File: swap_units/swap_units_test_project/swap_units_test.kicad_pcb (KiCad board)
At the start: 2 copper layers, 12 parts, among them U1 LM324, U2 PIC18F452-IP, U3 LM324

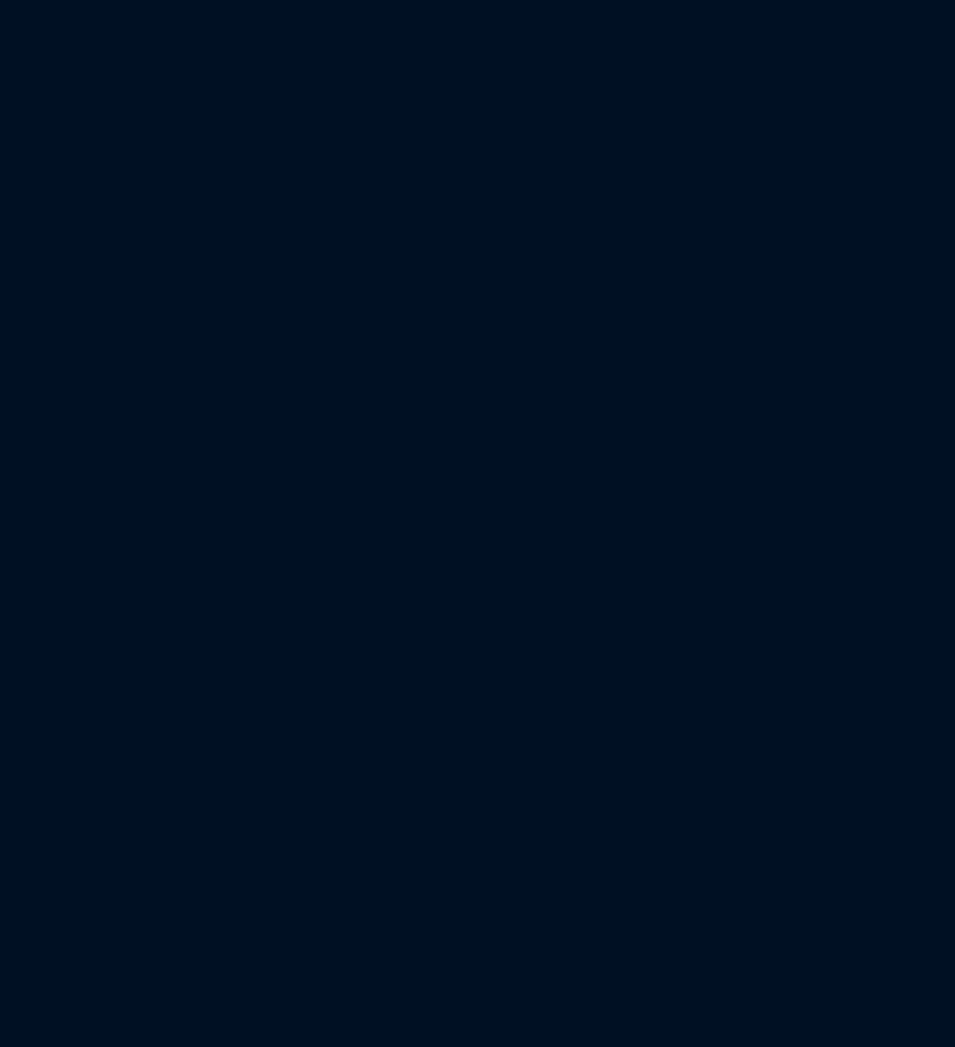
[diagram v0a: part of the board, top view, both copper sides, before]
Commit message: Moved and modified test project
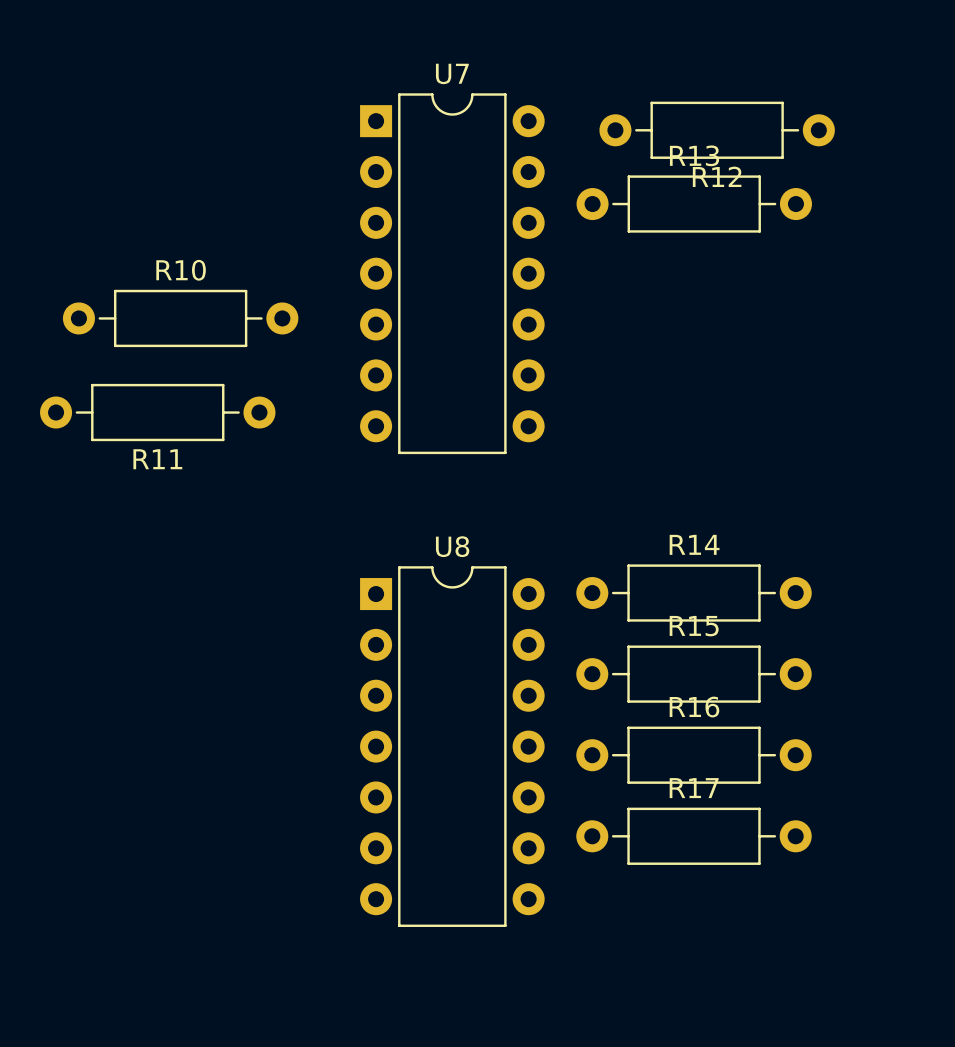
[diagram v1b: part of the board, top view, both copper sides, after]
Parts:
- added R10: R, Resistor_THT:R_Axial_DIN0207_L6.3mm_D2.5mm_P10.16mm_Horizontal, F.Cu at (21.1, 62.4)
- added R11: R, Resistor_THT:R_Axial_DIN0207_L6.3mm_D2.5mm_P10.16mm_Horizontal, F.Cu at (30.1, 67.1)
- added R12: R, Resistor_THT:R_Axial_DIN0207_L6.3mm_D2.5mm_P10.16mm_Horizontal, F.Cu at (58.0, 53.0)
- added R13: R, Resistor_THT:R_Axial_DIN0207_L6.3mm_D2.5mm_P10.16mm_Horizontal, F.Cu at (46.7, 56.6)
- added R14: R, Resistor_THT:R_Axial_DIN0207_L6.3mm_D2.5mm_P10.16mm_Horizontal, F.Cu at (46.7, 76.1)
- added R15: R, Resistor_THT:R_Axial_DIN0207_L6.3mm_D2.5mm_P10.16mm_Horizontal, F.Cu at (46.7, 80.1)
- added R16: R, Resistor_THT:R_Axial_DIN0207_L6.3mm_D2.5mm_P10.16mm_Horizontal, F.Cu at (46.7, 84.2)
- added R17: R, Resistor_THT:R_Axial_DIN0207_L6.3mm_D2.5mm_P10.16mm_Horizontal, F.Cu at (46.7, 88.2)
- added U7: LM324, Package_DIP:DIP-14_W7.62mm, F.Cu at (35.9, 52.5)
- added U8: LM324, Package_DIP:DIP-14_W7.62mm, F.Cu at (35.9, 76.1)

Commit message: updated test projects
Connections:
- U7 pad 13: /Level1/Level3a/out_level_2 -> /Level1/Level3a/out_level_1
- U7 pad 14: /Level1/Level3a/out_level_2 -> /Level1/Level3a/out_level_1
- U8 pad 13: /Level1/Level3b/out_level_2 -> /Level1/Level3b/out_level_1
- U8 pad 14: /Level1/Level3b/out_level_2 -> /Level1/Level3b/out_level_1
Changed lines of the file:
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@@
     (zones 0)
     (modules 22)
-    (nets 54)
+    (nets 56)
   )
   (page A4)
@@
   (net 52 /Level1/Level3a/out_level_2)
   (net 53 /Level1/Level3b/out_level_2)
+  (net 54 /Level1/Level3a/out_level_1)
+  (net 55 /Level1/Level3b/out_level_1)
   (net_class Default "This is the default net class."
     (clearance 0.2)
@@
     (add_net +5V)
     (add_net /Level1/Level2b/out_level_2)
+    (add_net /Level1/Level3a/out_level_1)
     (add_net /Level1/Level3a/out_level_2)
+    (add_net /Level1/Level3b/out_level_1)
     (add_net /Level1/Level3b/out_level_2)
     (add_net /Level1/out_level_1)
@@
     (fp_arc (start 3.81 -1.33) (end 2.81 -1.33) (angle -180) (layer F.SilkS) (width 0.12))
     (pad 14 thru_hole oval (at 7.62 0) (size 1.6 1.6) (drill 0.8) (layers *.Cu *.Mask)
-      (net 53 /Level1/Level3b/out_level_2))
+      (net 55 /Level1/Level3b/out_level_1))
     (pad 7 thru_hole oval (at 0 15.24) (size 1.6 1.6) (drill 0.8) (layers *.Cu *.Mask)
       (net 53 /Level1/Level3b/out_level_2))
     (pad 13 thru_hole oval (at 7.62 2.54) (size 1.6 1.6) (drill 0.8) (layers *.Cu *.Mask)
-      (net 53 /Level1/Level3b/out_level_2))
+      (net 55 /Level1/Level3b/out_level_1))
     (pad 6 thru_hole oval (at 0 12.7) (size 1.6 1.6) (drill 0.8) (layers *.Cu *.Mask)
       (net 53 /Level1/Level3b/out_level_2))
@@
     (fp_arc (start 3.81 -1.33) (end 2.81 -1.33) (angle -180) (layer F.SilkS) (width 0.12))
     (pad 14 thru_hole oval (at 7.62 0) (size 1.6 1.6) (drill 0.8) (layers *.Cu *.Mask)
-      (net 52 /Level1/Level3a/out_level_2))
+      (net 54 /Level1/Level3a/out_level_1))
     (pad 7 thru_hole oval (at 0 15.24) (size 1.6 1.6) (drill 0.8) (layers *.Cu *.Mask)
       (net 52 /Level1/Level3a/out_level_2))
     (pad 13 thru_hole oval (at 7.62 2.54) (size 1.6 1.6) (drill 0.8) (layers *.Cu *.Mask)
-      (net 52 /Level1/Level3a/out_level_2))
+      (net 54 /Level1/Level3a/out_level_1))
     (pad 6 thru_hole oval (at 0 12.7) (size 1.6 1.6) (drill 0.8) (layers *.Cu *.Mask)
       (net 52 /Level1/Level3a/out_level_2))
